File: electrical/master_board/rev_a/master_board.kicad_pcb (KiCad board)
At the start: 2 copper layers, 145.3 x 156.6 mm, 213 parts, among them CN1 USB3140-30-230-1-C;VERT,2.3FL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, CN10 WOW_OUT;M2x6S, CN2 USB3140-30-230-1-C;VERT,2.3FL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, CN5 LIDAR_ADAPTER;2xF1x3+F1x2, CN6 SERVO;F1x3, CN7 SERVO;F1x3, CN8 SERVO;F1x3, CN81 HCSR04LP;F1X4, CN82 HCSR04LP;F1X4, CN83 HCSR04LP;F1X4, CN84 HCSR04LP;F1X4, CN85 HCSR04LP;F1X4, CN86 HCSR04LP;F1X4, CN87 HCSR04LP;F1X4, CN88 MIKROBUS_MATE;SMALL, CN89 MIKROBUS_MATE;MEDIUM, CN9 SERVO;F1x3, CN90 STADAPTER;F2x4, CN91 HR2_ENCODER;2xF1x3, CN92 HR2_ENCODER;2xF1x3, CN93 POLOLU_U3V70F9;F1x4+F1x5, CN94 RASPI;F2X20, CN95 NUCLEO-F767ZI;2xF2x35, Q1 2N2222;SOT23, Q10 2N7000;SOT23, Q11 2N7000;SOT23, Q12 2N7000;SOT23, Q13 2N7000;SOT23, Q14 2N7000;SOT23, Q15 2N7000;SOT23, Q16 2N7000;SOT23, Q17 2N7000;SOT23, Q18 2N7000;SOT23, Q19 2N7000;SOT23, Q2 POWER_PFET_GSD, Q20 2N7000;SOT23, Q21 PFET_6A_GSD;SOT23, Q22 2N7000;SOT23, Q3 2N2222;SOT23, Q4 2N7000;SOT23, Q5 2N7000;SOT23, Q6 2N7000;SOT23, Q7 2N7000;SOT23, Q8 2N7000;SOT23, Q9 2N7000;SOT23, SW1 BUTTON;6x3.5, SW2 BUTTON;6x3.5, SW3 BUTTON;6x3.5, U1 LM66100;SOT363, U10 CD450B;TTSOP16, U11 SN74HCS595;TTSOP16, U12 SN74HCS595;TTSOP16, U13 74LVC1G11;SOT363, U14 MCP2542;SOIC8, U15 MCP2542;SOIC8, U16 74LVC1G74;TSSOP8, U17 CPC1017N;SOP4W3.8L4.1, U18 CPC1017N;SOP4W3.8L4.1, U2 MCP7940;SOIC8, U3 CAT24C32;SOIC8, U4 DRV8833PWPR;16HTSSOP, U5 SN74HCS595;TTSOP16, U6 SN74HCS166;TTSOP16, U7 SN74HCS166;TTSOP16, U8 SN74HCS595;TTSOP16, U9 CD450B;TTSOP16, X1 32.768kHz9pF;3.2x1.5

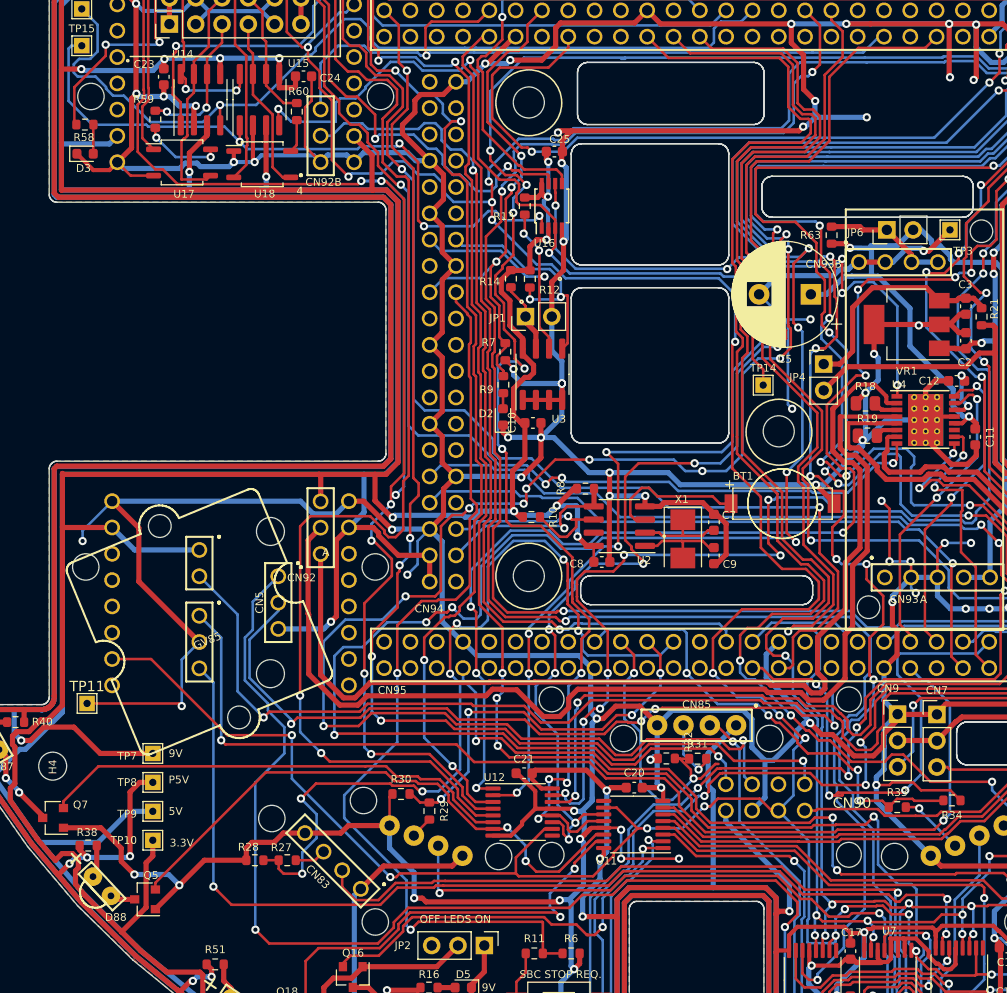
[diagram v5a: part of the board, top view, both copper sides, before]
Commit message: Added RasPi Display On/Off Circuit.
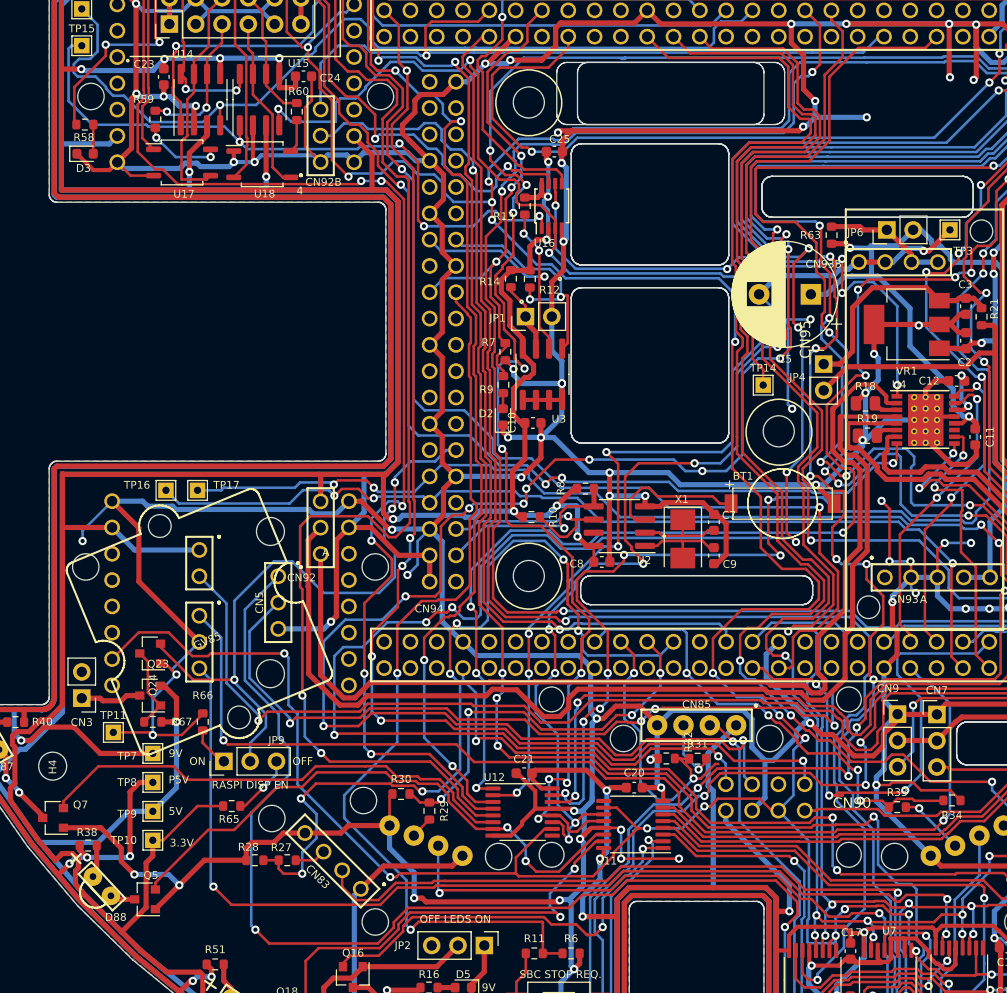
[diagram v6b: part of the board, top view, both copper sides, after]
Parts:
- added CN3: RPI_DSP_PWR;M1x2, Connector_PinHeader_2.54mm:PinHeader_1x02_P2.54mm_Vertical, F.Cu at (40.6, 135.4)
- added JP9: RPI_DISP_EN;M1x3, Connector_PinHeader_2.54mm:PinHeader_1x03_P2.54mm_Vertical, F.Cu at (54.4, 141.5)
- added Q23: POWER_PFET_GSD, Package_TO_SOT_SMD:SOT-23, F.Cu at (47.2, 135.1)
- added Q24: 2N7000;SOT23, Package_TO_SOT_SMD:SOT-23, F.Cu at (47.2, 131.1)
- added R65: 100KΩ;1608, Resistor_SMD:R_0603_1608Metric, F.Cu at (55.1, 145.8)
- added R66: 100KΩ;1608, Resistor_SMD:R_0603_1608Metric, F.Cu at (52.3, 137.7)
- added R67: 100KΩ;1608, Resistor_SMD:R_0603_1608Metric, F.Cu at (47.5, 137.7)
- added TP16: SPC_TX;M1x2, TestPoint:TestPoint_THTPad_1.5x1.5mm_Drill0.7mm, F.Cu at (48.8, 115.3)
- added TP17: SBC_RX;M1x2, TestPoint:TestPoint_THTPad_1.5x1.5mm_Drill0.7mm, F.Cu at (51.8, 115.3)
- moved TP11 3.78 mm to (43.7, 138.7)
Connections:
- CN94 pad 11: Net-(CN94-Pad11) -> /Single Board Computer/RPI_DSP_EN
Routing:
- net /Single Board Computer/RPI_DSP_EN: track 0.00 -> 62.6 mm, vias 0 -> 3
- net /LED's/LED5: track 174.6 -> 142.3 mm, vias 7 -> 6
- net /SPBC_TX: track 64.5 -> 92.2 mm, vias 1 -> 3
- net /SPBC_RX: track 71.7 -> 95.7 mm, vias 2 -> 4
- net /5V: track 823.6 -> 838.8 mm, vias 16 -> 17
- net /3.3V: track 819.4 -> 827.7 mm
- net Net-(Q23-Pad1): track 0.00 -> 8.08 mm
- net /GND: track 1606.6 -> 1613.3 mm, vias 129 -> 130
- net /~NRST: track 373.6 -> 380.2 mm
- net Net-(JP9-Pad3): track 0.00 -> 6.03 mm, vias 0 -> 1
- net Net-(CN3-Pad1): track 0.00 -> 5.92 mm
- net Net-(JP9-Pad1): track 0.00 -> 4.17 mm
- net /LED's/LED7: track 46.1 -> 47.2 mm
- net /LDR_TX: track 106.8 -> 107.5 mm
- net /Connectors/LDR_EN: track 138.7 -> 139.4 mm
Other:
- outline, holes or cut-outs redrawn
- board text added: "OFF"
- board text added: "ON"
- board text added: "RASPI DISP EN"

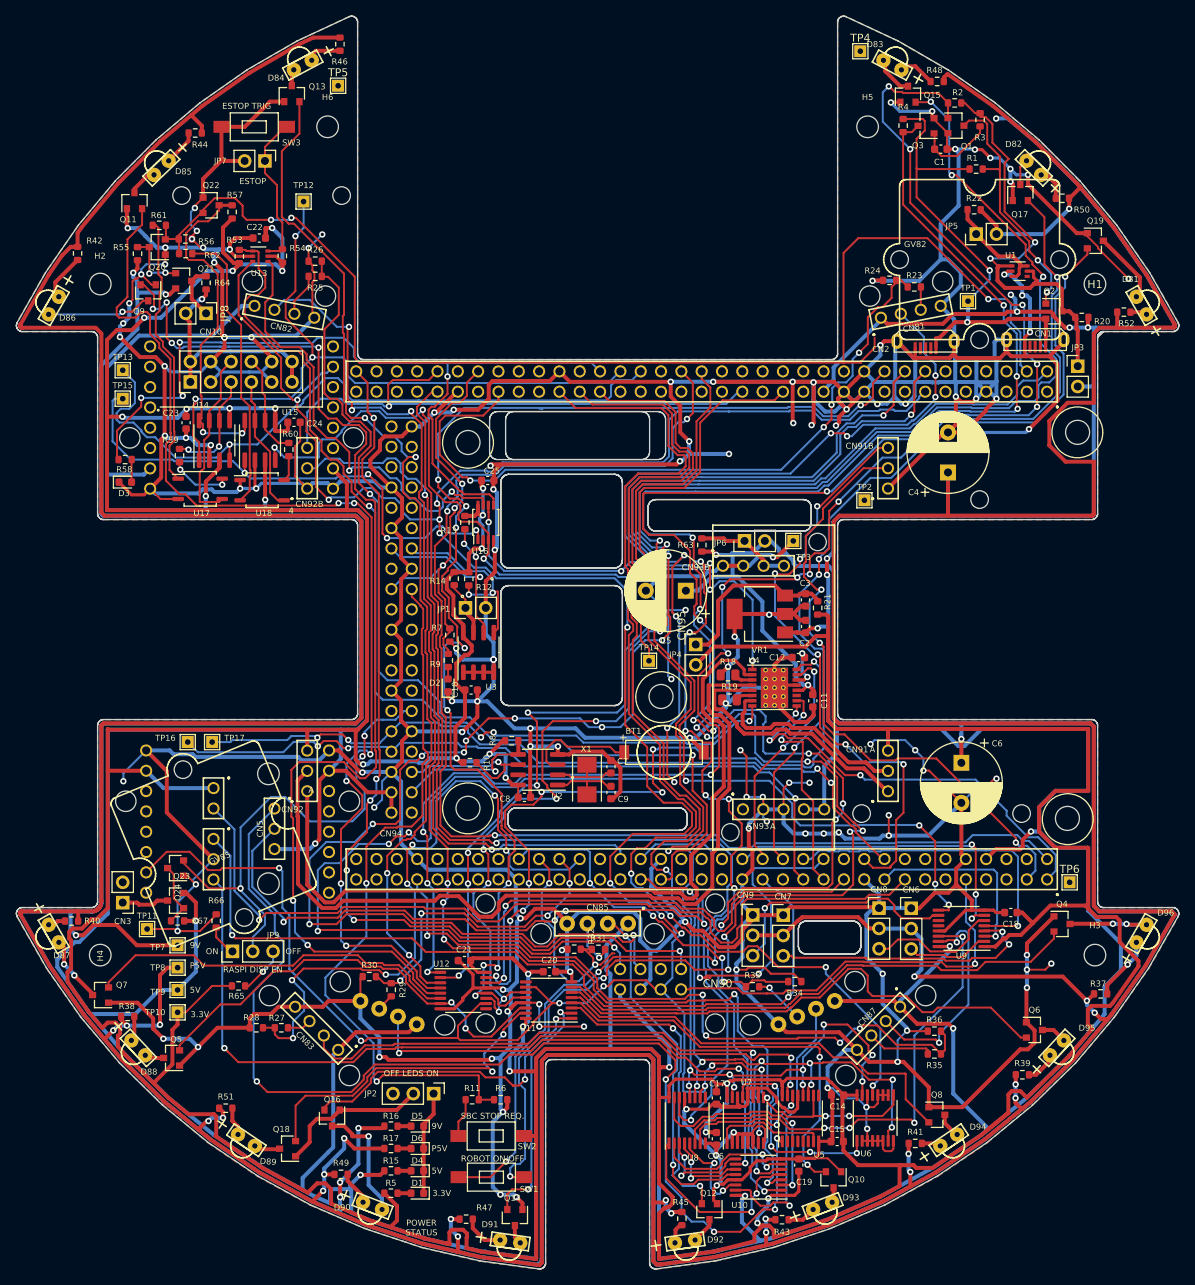
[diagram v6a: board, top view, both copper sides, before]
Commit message: Got servo current/possition stuff merged in.
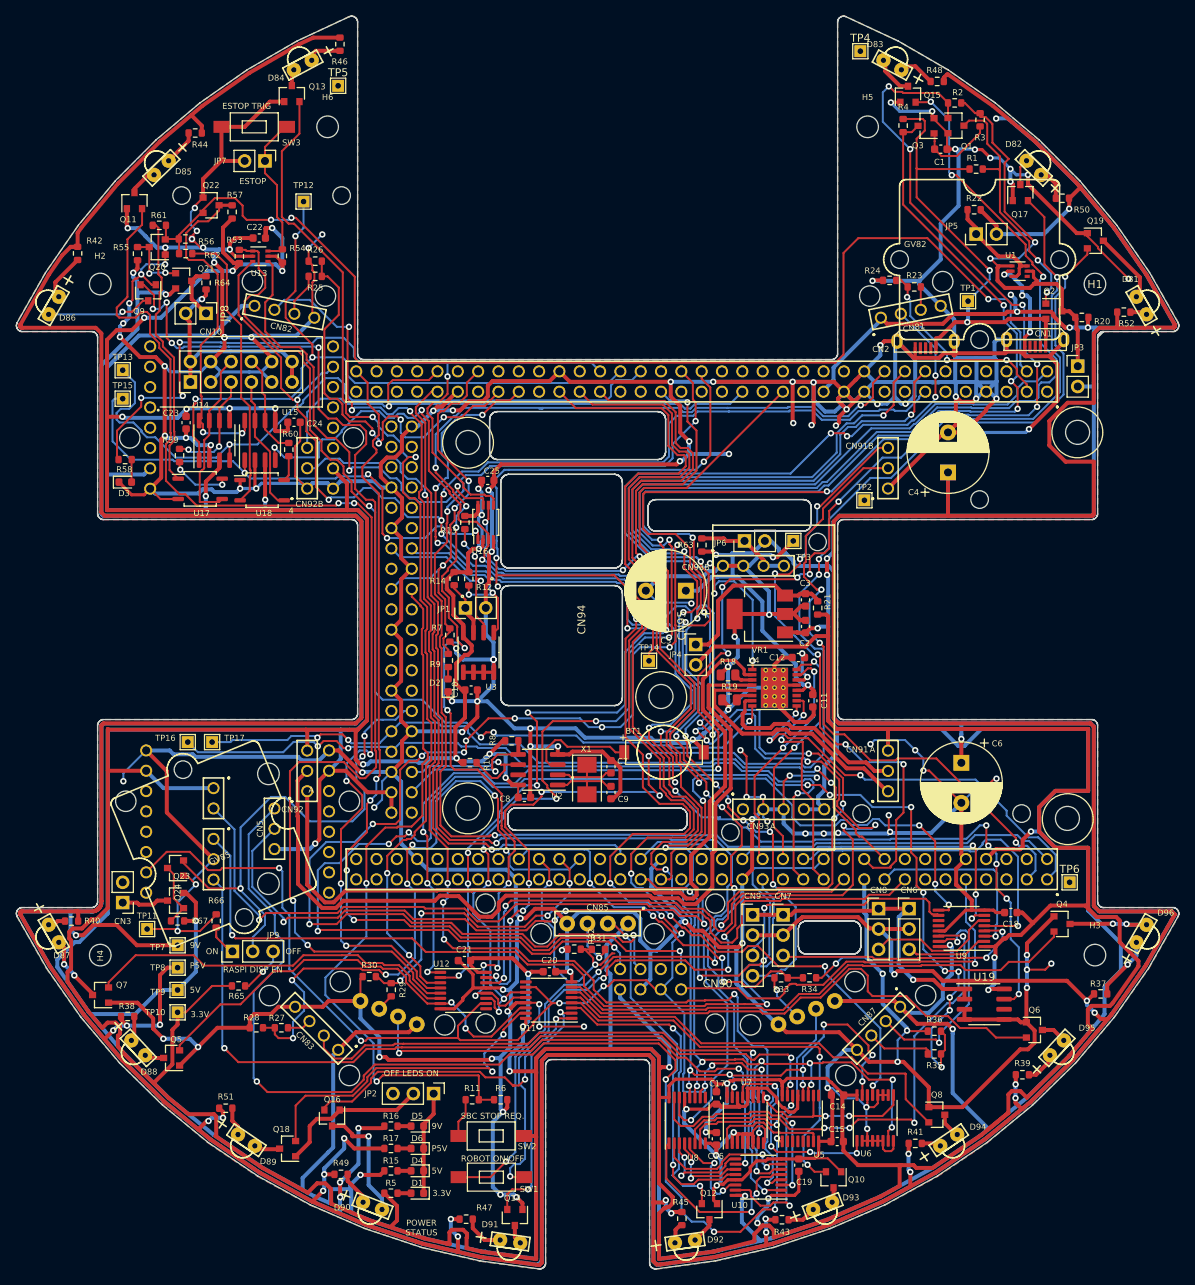
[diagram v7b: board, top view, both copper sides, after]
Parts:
- added U19: ACS711;SOIC8, Package_SO:SOIC-8_3.9x4.9mm_P1.27mm, F.Cu at (148.3, 148.1)
- CN6, CN7, CN8: value SERVO;F1x3 -> SERVO;M1x3
- CN9: value SERVO;F1x3 -> SERVO;M1x4; footprint Connector_PinHeader_2.54mm:PinHeader_1x03_P2.54mm_Vertical -> Connector_PinHeader_2.54mm:PinHeader_1x04_P2.54mm_Vertical
- moved R33 3.74 mm to (122.9, 144.8), turned to 180 degrees
- moved R34 1.90 mm to (126.5, 144.8)
- moved CN6 0.27 mm to (138.9, 136.1)
- moved CN8 0.09 mm to (135.1, 136.1)
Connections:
- CN6 pad 1: /GND -> /Sonars and Servos/SGND
- CN7 pad 1: /GND -> /Sonars and Servos/SGND
- CN8 pad 1: /GND -> /Sonars and Servos/SGND
- CN9 pad 1: /GND -> /Sonars and Servos/SGND
- CN95 pad 1104: /INT0 -> /ECHO1
- CN95 pad 1135: /~ESTOP_CLR -> /SERVO_CUR
- CN95 pad 1140: Net-(CN95-Pad1140) -> /~ESTOP_CLR
- CN95 pad 1154: Net-(CN95-Pad1154) -> /SERVO_POS
- CN95 pad 1156: /ECHO7 -> /ECHO2
- CN95 pad 1240: /ECHO2 -> /ECHO7
- CN95 pad 1264: /ECHO1 -> /INT0
- R23 pad 1: /ECHO7 -> /ECHO1
- R24 pad 2: /ECHO7 -> /ECHO1
- R35 pad 1: /ECHO1 -> /ECHO7
- R36 pad 2: /ECHO1 -> /ECHO7
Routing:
- net /SERVO_CUR: track 0.00 -> 174.9 mm, vias 0 -> 11
- net /SERVO_POS: track 0.00 -> 124.9 mm, vias 0 -> 9
- net /ECHO2: track 123.2 -> 51.4 mm, vias 2 -> 4
- net /ECHO1: track 87.1 -> 25.6 mm, vias 5 -> 3
- net /Sonars and Servos/SGND: track 0.00 -> 38.9 mm, vias 0 -> 1
- net /GND: track 1613.3 -> 1578.3 mm, vias 130 -> 129
- net /Power/PWR_SW_A: track 267.3 -> 277.8 mm
- net /3.3V: track 827.7 -> 835.9 mm, vias 23 -> 25
- net /WOW_EN: track 160.6 -> 154.0 mm
- net /SPBC_TX: track 92.2 -> 97.9 mm
- net /SWCLK: track 192.5 -> 196.7 mm
- net /5V: track 838.8 -> 843.0 mm
- net /SWDIO: track 191.6 -> 194.2 mm
- net /ECHO6: track 45.7 -> 48.3 mm
- net /P5V: track 801.5 -> 803.8 mm
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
